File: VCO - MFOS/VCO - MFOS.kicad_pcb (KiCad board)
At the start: 2 copper layers, 127 x 101.6 mm, 121 parts, among them J1 CV1, J10 PWM_CV, J11 SQU, J12 RV1P2, J13 RV2P2, J14 RV1P1, J15 RV2P1, J16 RV2P3, J17 RV1P3, J18 RV10P3, J19 RV10P1, J2 CV2, J20 RV10P2, J21 GND_CONN, J22 +12V_CONN, J23 -12V_CONN, J3 CV3, J4 CV4, J5 LIN, J6 SYNC, J7 RMP, J8 TRI, J9 SIN, Q1 SSM2210, Q2 Q_PJFET_GSD, U1 OP275, U2 TL072, U3 TL074, U4 LM13700, U5 TL072, U6 TL071

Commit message: whoops
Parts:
- removed RV1, RV2: 100k, Connector_Wire:SolderWirePad_1x03_P3.175mm_Drill1mm
- removed RV10: 100K, Connector_Wire:SolderWirePad_1x03_P3.175mm_Drill1mm
- Q2: value Q_PJFET_GSD -> Q_PJFET_DSG; footprint Package_TO_SOT_THT:TO-92 -> Package_TO_SOT_THT:TO-92L_Inline_Wide
- moved J7 92.0 mm to (34.3, 81.3), turned to 270 degrees
- moved R33 76.8 mm to (37.3, 81.3), turned to 0 degrees
- moved J8 75.1 mm to (43.7, 87.4), turned to 270 degrees
- moved J9 68.7 mm to (97.6, 81.0), turned to 20 degrees
- moved R43 58.8 mm to (98.6, 83.7), turned to 290 degrees
- moved R41 50.9 mm to (46.7, 87.4)
- moved R39 48.0 mm to (59.7, 95.8), turned to 0 degrees
- moved R38 47.1 mm to (89.8, 108.8), turned to 110 degrees
- moved U4 46.9 mm to (81.0, 98.3), turned to 110 degrees
- moved R34 45.2 mm to (92.8, 107.7), turned to 110 degrees
- moved R44 44.6 mm to (108.2, 99.4), turned to 110 degrees
- moved R32 44.1 mm to (93.1, 99.4), turned to 290 degrees
- moved C15 43.1 mm to (95.3, 67.2), turned to 0 degrees
- moved RV9 42.2 mm to (109.5, 107.3), turned to 270 degrees
- moved R36 42.1 mm to (59.7, 92.5), turned to 0 degrees
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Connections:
- Q1 pad 1: Net-(C2-Pad1) -> Net-(C3-Pad1)
- Q1 pad 2: Net-(D1-Pad2) -> Earth
- Q1 pad 7: Earth -> Net-(D1-Pad2)
- Q1 pad 8: Net-(C3-Pad1) -> Net-(C2-Pad1)
- Q2 pad 1: Net-(Q2-Pad1) -> Net-(C3-Pad1)
- Q2 pad 3: Net-(C3-Pad1) -> Net-(Q2-Pad3)
- R18 pad 2: Net-(Q2-Pad1) -> Net-(Q2-Pad3)
- R32 pad 2: Net-(R32-Pad2) -> Earth
- U4 pad 4: Net-(R32-Pad2) -> Earth
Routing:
- net -12V: track 0.00 -> 483.1 mm, vias 0 -> 1
- net Earth: track 0.00 -> 462.0 mm
- net +12V: track 0.00 -> 382.0 mm
- net Net-(C14-Pad2): track 0.00 -> 136.7 mm
- net Net-(C12-Pad1): track 0.00 -> 88.7 mm
- net Net-(C11-Pad1): track 0.00 -> 68.8 mm, vias 0 -> 1
- net Net-(C6-Pad1): track 0.00 -> 60.8 mm
- net Net-(C6-Pad2): track 0.00 -> 56.8 mm
- net Net-(R22-Pad1): track 0.00 -> 56.2 mm
- net Net-(C2-Pad1): track 0.00 -> 54.8 mm
- net Net-(C1-Pad2): track 0.00 -> 53.4 mm
- net Net-(C2-Pad2): track 0.00 -> 51.4 mm
- net Net-(J10-Pad1): track 0.00 -> 49.0 mm
- net Net-(D4-Pad2): track 0.00 -> 46.6 mm
- net RAW: track 0.00 -> 45.3 mm
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- added copper zone on B.Cu, net (none)
- added copper zone on F.Cu, net (none)
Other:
- net class Default: clearance 0.2 -> 0.5
- rule trace_clearance: 0.2 -> 0.5
- rule via_min_size: 0.4 -> 0.6
- board text added: "+12V"
- board text added: "-12V"
- board text added: "1V/OCT"
- board text added: "CV1"
- board text added: "CV2"
- board text added: "CV3"
- board text added: "CV4"
- board text added: "CourseP1"
- board text added: "CourseP3"
- board text added: "Crs2"
- board text added: "Fin2"
- board text added: "FineP1"
- board text added: "FineP3"
- board text added: "GND"
- board text added: "HF TRIM"
- board text added: "LM13700"
- board text added: "Lin"
- board text added: "MFOS"
- board text added: "PW1"
- board text added: "PW2"
- board text added: "PW3"
- board text added: "PWM_CV"
- board text added: "RMP"
- board text added: "SIN"
- board text added: "SQU"
- board text added: "SSM2210"
- board text added: "SawOff"
- board text added: "SinBias"
- board text added: "SinLvl"
- board text added: "SinShape"
- board text added: "Sync"
- board text added: "TL071"
- board text added: "TL072"
- board text added: "TL074"
- board text added: "TRI"
- board text added: "TriOff"
- board text added: "VO TRIM"

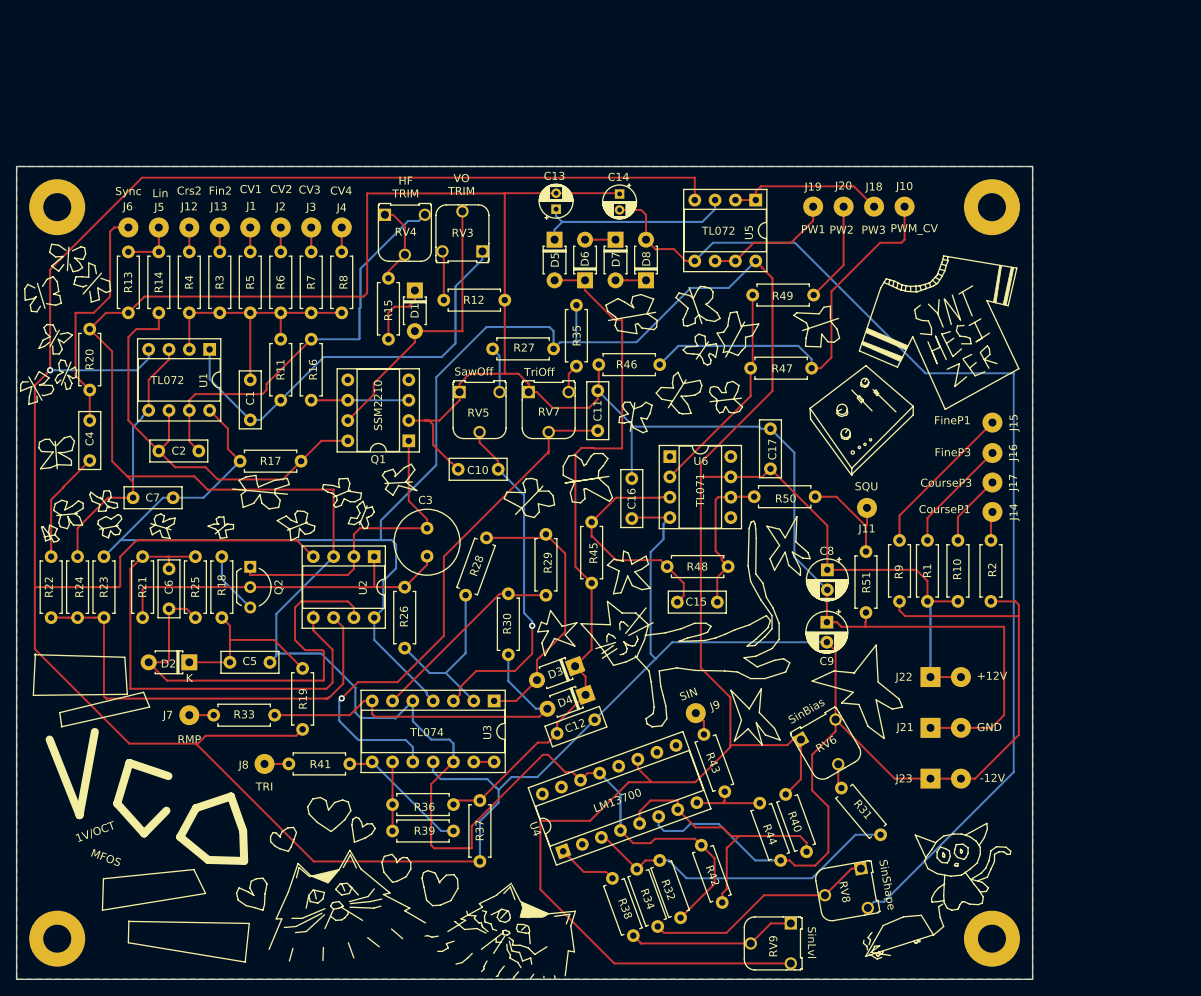
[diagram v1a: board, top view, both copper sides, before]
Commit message: fixed error and rerouted VCO
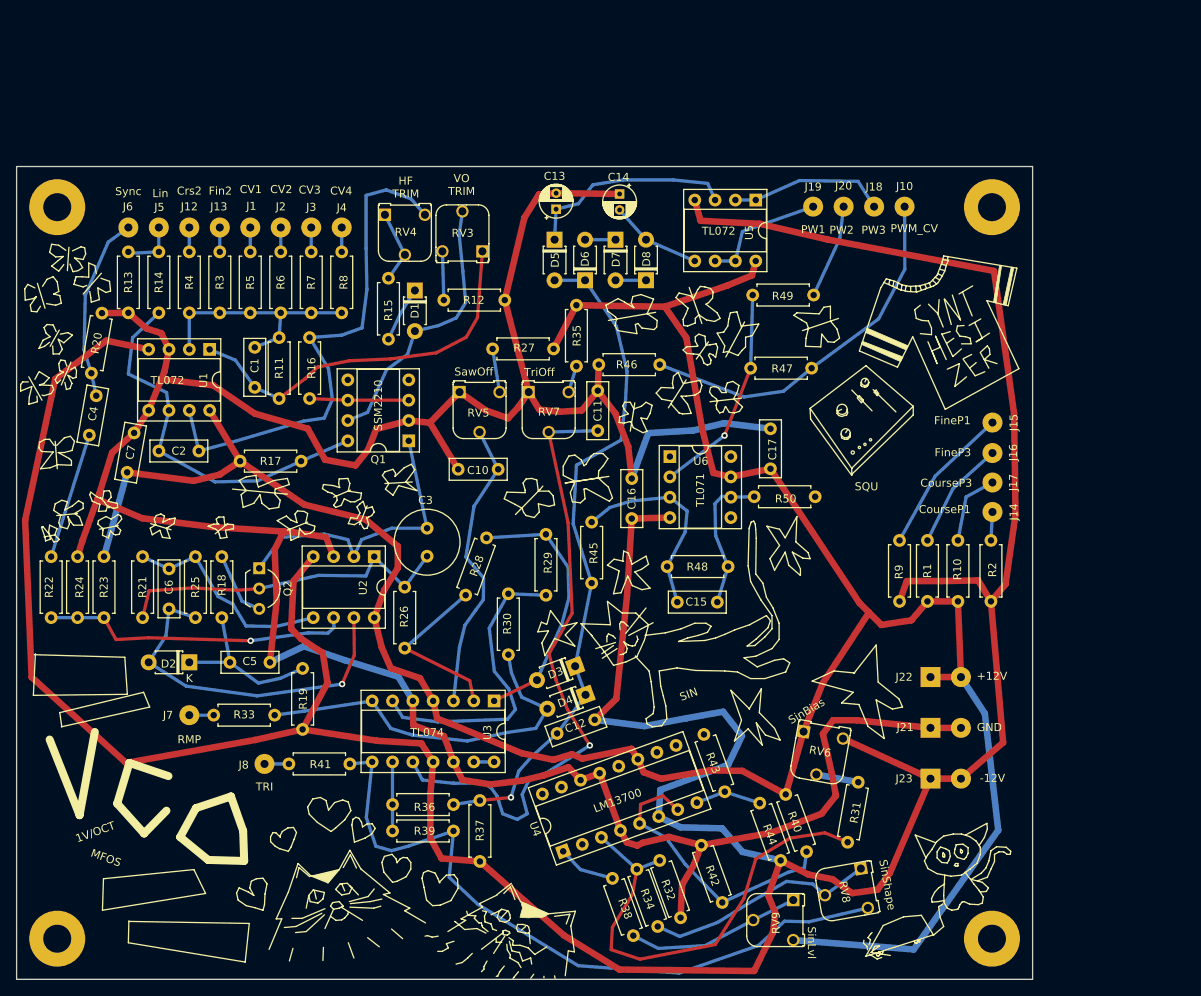
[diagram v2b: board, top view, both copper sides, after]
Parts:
- removed C8, C9: 10uF, Capacitor_THT:CP_Radial_D5.0mm_P2.50mm
- removed J11: SQU, Connector_Wire:SolderWirePad_1x01_Drill1mm
- removed J9: SIN, Connector_Wire:SolderWirePad_1x01_Drill1mm
- removed R51: 3K, Resistor_THT:R_Axial_DIN0207_L6.3mm_D2.5mm_P7.62mm_Horizontal
- moved C7 6.56 mm to (26.5, 50.9), turned to 80 degrees
- moved C1 4.10 mm to (42.5, 35.3)
- moved C4 3.20 mm to (22.7, 41.4), turned to 260 degrees
- moved RV9 2.94 mm to (109.8, 104.4)
- moved R31 2.23 mm to (117.9, 89.7), turned to 260 degrees
- moved R20 2.12 mm to (22.0, 38.5), turned to 80 degrees
- moved Q2 1.13 mm to (43.0, 62.9)
- moved RV6 1.04 mm to (111.1, 83.3), turned to 350 degrees
- moved R16 0.29 mm to (49.3, 34.1)
- moved R11 0.29 mm to (45.5, 41.7)
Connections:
- RV8 pad 3: Net-(C14-Pad2) -> Net-(R39-Pad2)
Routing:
- net Net-(C14-Pad2): track 136.7 -> 11.6 mm
- net Earth: track 462.0 -> 360.3 mm
- net Net-(R39-Pad2): track 16.6 -> 87.4 mm
- net +12V: track 382.0 -> 315.9 mm
- net Net-(C6-Pad1): track 60.8 -> 26.8 mm
- net -12V: track 483.1 -> 454.2 mm, vias 1 -> 0
- net Net-(R22-Pad1): track 56.2 -> 38.6 mm, vias 0 -> 1
- net Net-(R31-Pad2): track 40.2 -> 57.7 mm
- net Net-(J11-Pad1): track 13.4 -> 0.00 mm
- net Net-(R29-Pad2): track 24.8 -> 37.7 mm
- net Net-(C2-Pad2): track 51.4 -> 64.3 mm
- net Net-(C6-Pad2): track 56.8 -> 44.7 mm, vias 0 -> 1
- net Net-(C11-Pad1): track 68.8 -> 79.2 mm
- net Net-(C2-Pad1): track 54.8 -> 47.6 mm
- net Net-(C4-Pad1): track 30.0 -> 23.1 mm
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- removed copper zone on B.Cu, net (none)
- removed copper zone on F.Cu, net (none)
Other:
- net class POWER added: clearance 0.5, trace_width 0.8128, via_dia 0.8, via_drill 0.4
- net class Traces added: clearance 0.5, trace_width 0.4064, via_dia 0.8, via_drill 0.4

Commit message: VCO - added tempco resistor holes
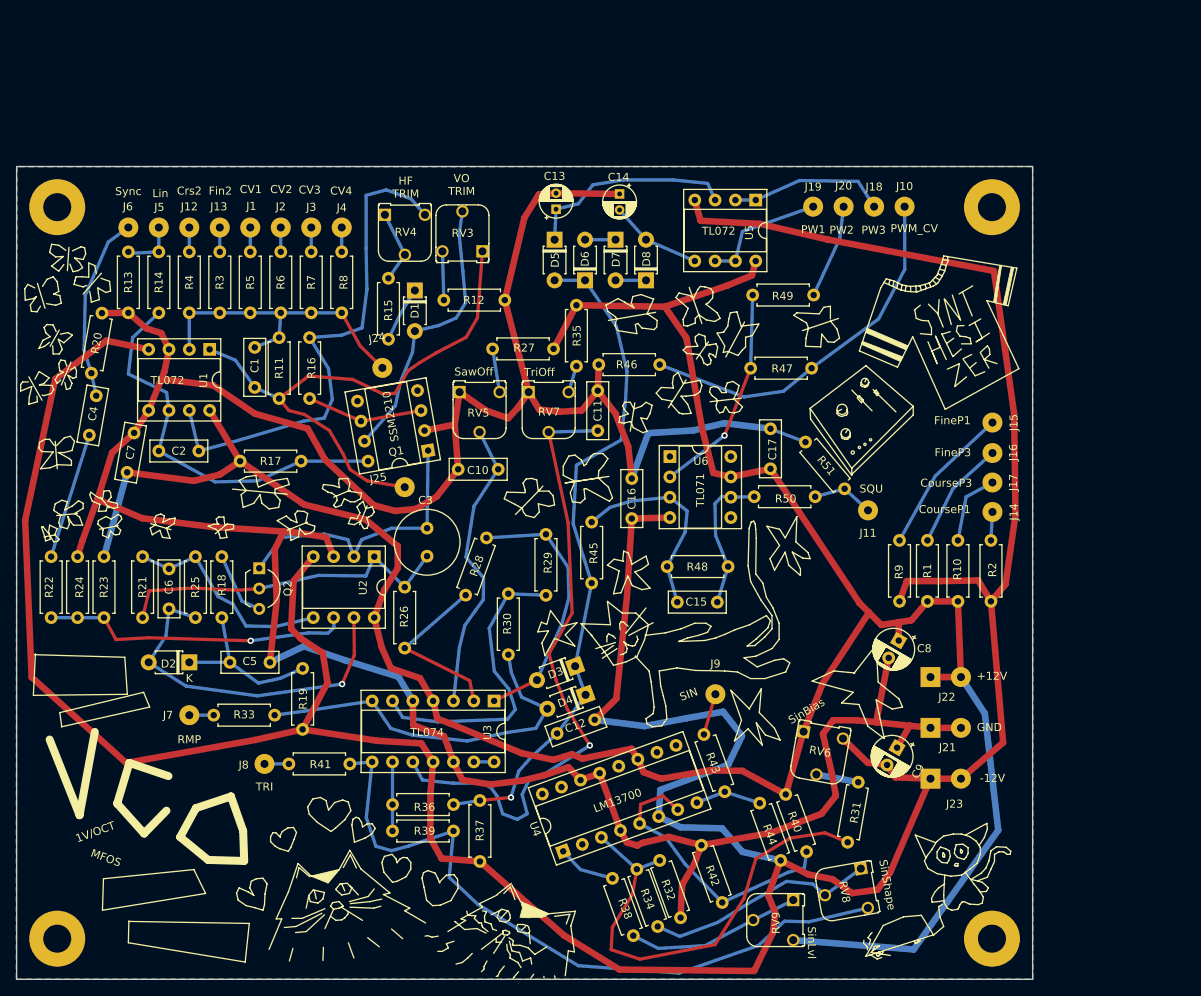
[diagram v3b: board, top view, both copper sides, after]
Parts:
- added C8: 10uF, Capacitor_THT:CP_Radial_D5.0mm_P2.50mm, F.Cu at (123.0, 72.0)
- added C9: 10uF, Capacitor_THT:CP_Radial_D5.0mm_P2.50mm, F.Cu at (122.8, 85.3)
- added J11: SQU, Connector_Wire:SolderWirePad_1x01_Drill1mm, F.Cu at (119.1, 55.7)
- added J24: R11_inv, Connector_Wire:SolderWirePad_1x01_Drill1mm, F.Cu at (58.4, 37.9)
- added J25: R11_out, Connector_Wire:SolderWirePad_1x01_Drill1mm, F.Cu at (61.2, 52.8)
- added J9: SIN, Connector_Wire:SolderWirePad_1x01_Drill1mm, F.Cu at (100.1, 78.7)
- added R51: 3K, Resistor_THT:R_Axial_DIN0207_L6.3mm_D2.5mm_P7.62mm_Horizontal, F.Cu at (116.2, 53.0)
- moved Q1 2.70 mm to (64.1, 48.2), turned to 190 degrees
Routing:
- net Net-(C1-Pad2): track 47.6 -> 70.2 mm
- net Earth: track 360.3 -> 382.8 mm
- net Net-(C1-Pad1): track 30.0 -> 38.6 mm
- net Net-(J11-Pad1): track 0.00 -> 7.79 mm
- net Net-(J9-Pad1): track 0.00 -> 5.23 mm
- net +12V: track 315.9 -> 318.2 mm
- net Net-(Q1-Pad3): track 12.4 -> 14.6 mm
- net Net-(C2-Pad1): track 47.6 -> 49.6 mm
- net Net-(C3-Pad1): track 37.4 -> 35.9 mm
- net -12V: track 454.2 -> 455.2 mm
- net Net-(D1-Pad2): track 34.0 -> 34.7 mm
- added copper zone on B.Cu, net Earth
- added copper zone on F.Cu, net Earth

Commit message: made silkscreens pretty
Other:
- board text added: "Rev:2"
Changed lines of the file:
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@@
   (general
     (thickness 1.6)
-    (drawings 1353)
+    (drawings 1354)
     (tracks 545)
     (zones 0)
@@
   )
   (setup
-    (last_trace_width 0.4064)
+    (last_trace_width 0.25)
     (user_trace_width 0.4064)
     (user_trace_width 0.8128)
@@
     )
   )
+  (gr_text "Rev:2\n" (at 31.3436 102.7684 10) (layer F.Cu)
+    (effects (font (size 1.5 1.5) (thickness 0.3)))
+  )
   (gr_line (start 120.9675 110.871) (end 120.9675 110.8075) (layer F.SilkS) (width 0.12))
